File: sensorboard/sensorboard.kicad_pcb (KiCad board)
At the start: 4 copper layers, 100 x 50 mm, 244 parts, among them J1 Conn_01x03, J10 Conn_01x02_Male, J11 Conn_01x05_Male, J12 Conn_01x03, J13 Conn_01x03, J14 USB_C_Receptacle_USB2.0, J2 Conn_01x03, J3 Conn_01x03, J4 Conn_01x03, J5 Conn_01x03, J6 Conn_01x03, J7 Conn_01x03, J8 Conn_01x03, J9 Conn_01x02_Male, Q1 MMDT2222A, U1 ESP32-PICO-D4, U10 MAX31856, U11 MAX31856, U12 RT9025-25GSP, U13 ADS1219, U14 ADS1219, U15 ADS1219, U16 MAX31856, U17 MAX31856, U18 MAX31856, U19 LTC4411, U2 LTC4411, U20 SN65HVD230, U3 TPS61092RSAR, U4 MAX31856, U5 MAX31856, U6 MAX31856, U7 MAX31856, U8 CP2102-GMR-QFN28, U9 MAX31856

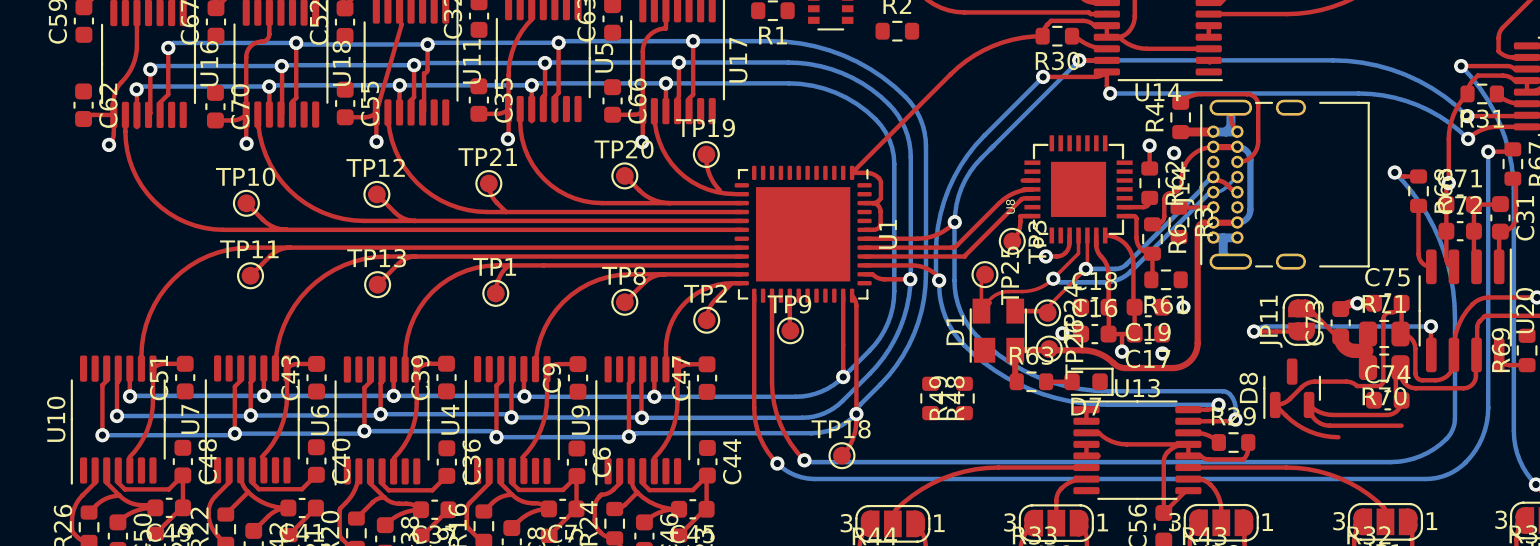
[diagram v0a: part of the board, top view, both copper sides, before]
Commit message: 3.3V connections and I2C capacitors
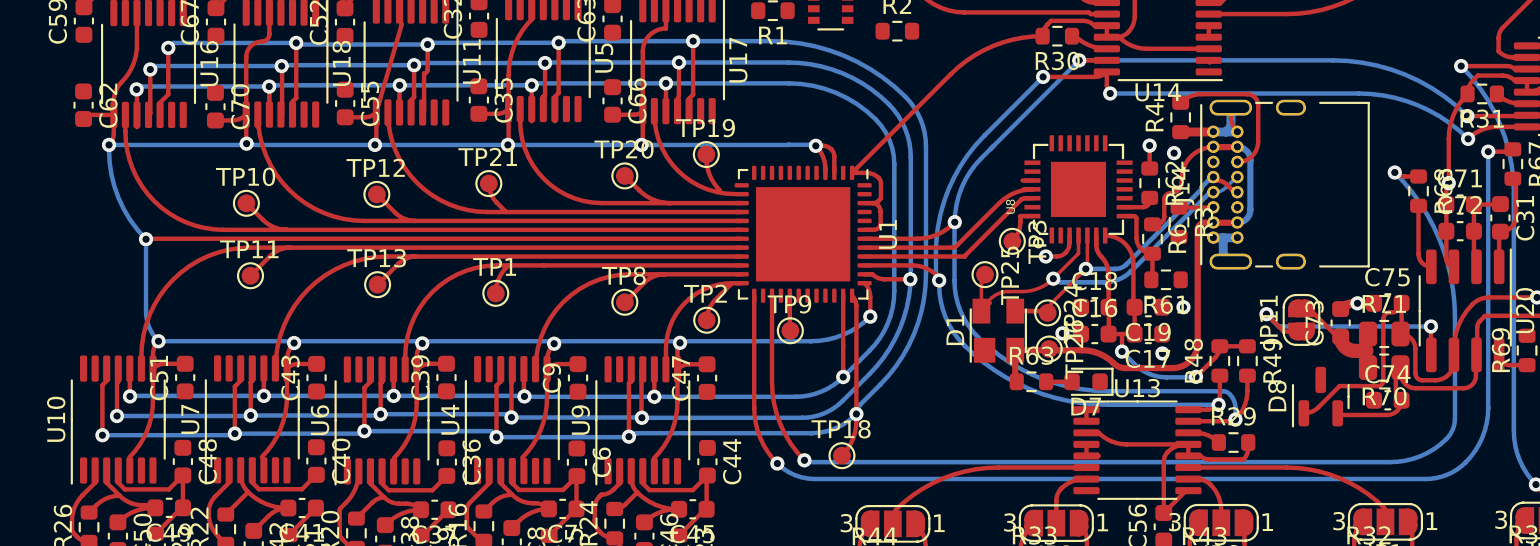
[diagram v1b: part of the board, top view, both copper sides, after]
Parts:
- moved R48 16.4 mm to (168.9, 61.7), turned to 90 degrees
- moved R49 16.0 mm to (170.5, 61.7), turned to -90 degrees
- moved D8 1.67 mm to (174.6, 63.7)
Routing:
- net +3V3: track 186.9 -> 334.9 mm, vias 8 -> 17
- net /CAN_HIGH: track 30.2 -> 22.7 mm
- net /CAN_LOW: track 36.2 -> 30.6 mm
- net /SDA: track 70.9 -> 73.5 mm
- net /SCL: track 68.2 -> 69.8 mm
- net /CAN/Vref: track 14.3 -> 13.5 mm

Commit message: update
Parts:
- moved R64 84.8 mm to (150.8, 85.9), turned to 180 degrees
- moved C24 83.5 mm to (167.3, 87.6), turned to 180 degrees
- moved U19 82.5 mm to (166.8, 90.2)
- moved U12 81.1 mm to (156.1, 88.2)
- moved C22 79.8 mm to (160.7, 88.5), turned to -90 degrees
- moved TP5 78.4 mm to (156.7, 48.7)
- moved C23 77.7 mm to (163.8, 88.4), turned to -90 degrees
- moved C20 77.4 mm to (150.7, 87.7)
- moved C21 76.7 mm to (150.7, 90.2)
- moved R66 74.1 mm to (162.9, 86.1)
- moved R65 67.4 mm to (162.3, 88.5), turned to 90 degrees
- moved C27 57.2 mm to (84.7, 61.8)
- moved C30 57.2 mm to (84.9, 63.7)
- moved C26 41.5 mm to (79.2, 62.3)
- moved C29 41.5 mm to (79.7, 64.5)
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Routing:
- net VBUS: track 34.2 -> 40.8 mm
- net Net-(C22-Pad2): track 0.00 -> 5.23 mm
- net Net-(C22-Pad1): track 0.00 -> 5.10 mm
- net Net-(R64-Pad1): track 0.00 -> 2.00 mm

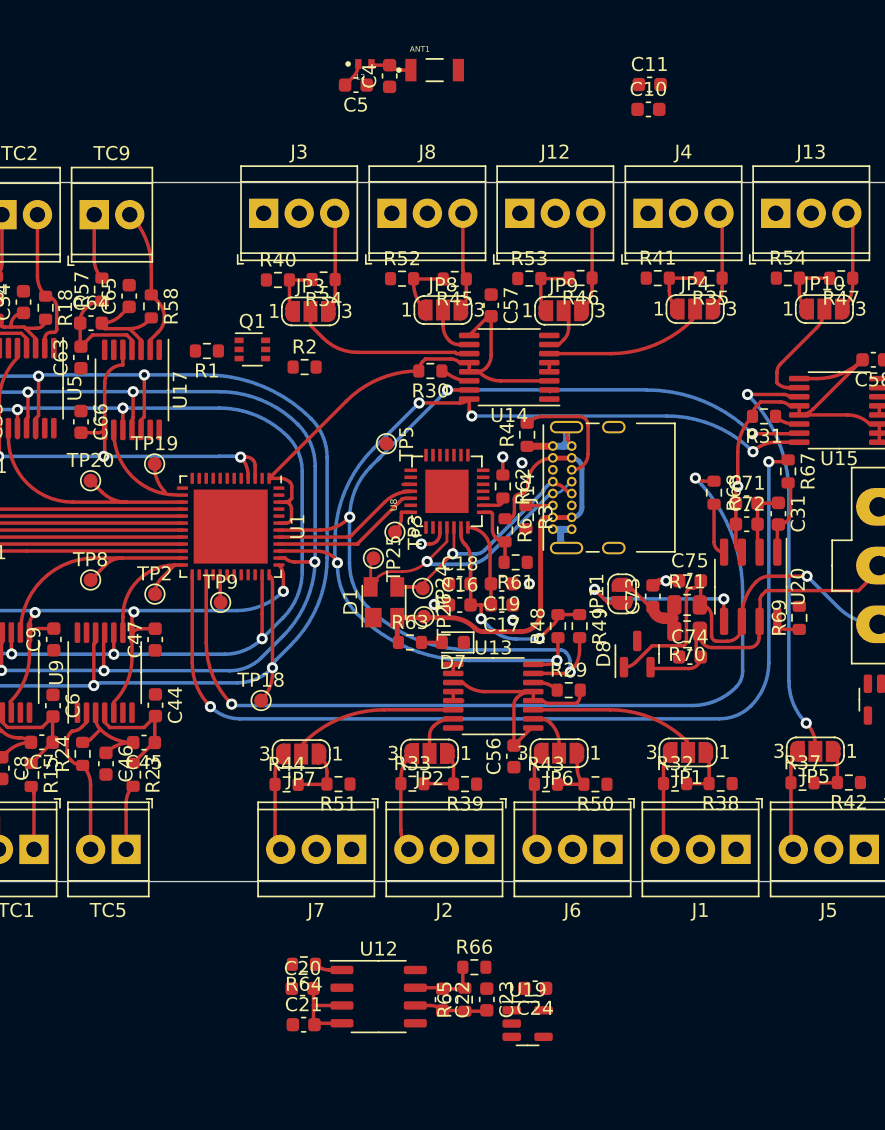
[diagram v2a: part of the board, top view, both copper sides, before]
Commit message: moved the U14 component and added component
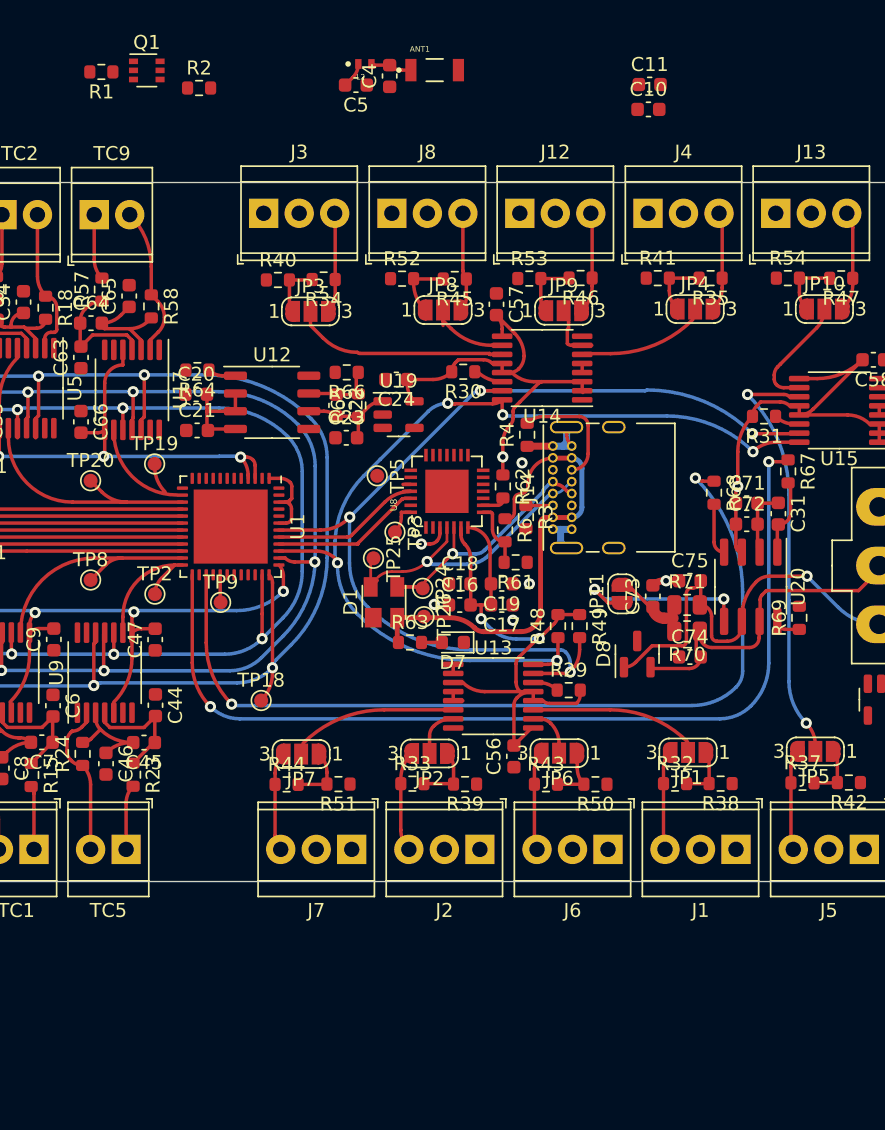
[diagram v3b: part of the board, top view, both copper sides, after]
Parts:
- moved C24 44.7 mm to (157.4, 44.1)
- moved U19 44.5 mm to (157.5, 46.6)
- moved R66 43.5 mm to (153.8, 43.6), turned to 180 degrees
- moved C22 43.2 mm to (153.1, 45.9)
- moved R64 43.2 mm to (143.1, 43.4)
- moved R65 43.2 mm to (154.7, 45.9)
- moved C20 43.2 mm to (143.1, 45.1)
- moved C21 43.2 mm to (143.1, 47.7)
- moved U12 43.2 mm to (148.5, 45.7)
- moved C23 41.4 mm to (153.8, 48.3), turned to 0 degrees
- moved R2 21.3 mm to (143.3, 23.2)
- moved Q1 21.3 mm to (139.5, 22.0)
- moved R1 21.3 mm to (136.3, 22.1)
- moved TP5 2.39 mm to (156.0, 51.0)
- moved U14 2.36 mm to (167.8, 43.3)
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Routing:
- net +3V3: track 334.9 -> 338.4 mm
- net /analogueI2C/AIN4: track 13.1 -> 15.6 mm
- net /analogueI2C/AIN6: track 10.9 -> 8.54 mm
- net /analogueI2C/AIN5: track 3.80 -> 5.87 mm
- net Net-(C22-Pad2): track 5.23 -> 7.29 mm
- net /SDA: track 73.5 -> 72.2 mm
- net VBUS: track 40.8 -> 42.1 mm
- net /analogueI2C/AIN7: track 3.43 -> 4.26 mm
- net /SCL: track 69.8 -> 69.3 mm

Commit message: transistor integration
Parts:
- moved TP6 142.5 mm to (156.5, 49.8)
- moved Q1 41.7 mm to (152.1, 61.8), turned to 90 degrees
- moved R1 41.6 mm to (149.8, 61.4), turned to 90 degrees
- moved R2 37.3 mm to (152.6, 59.3)
- moved L2 21.9 mm to (144.2, 40.4), turned to -90 degrees
- moved ANT1 20.6 mm to (144.6, 35.4), turned to 90 degrees
- moved C4 20.1 mm to (145.0, 38.6), turned to 180 degrees
- moved C5 20.1 mm to (145.7, 41.1), turned to -90 degrees
- moved TP9 10.7 mm to (153.9, 65.6)
- moved TP25 6.35 mm to (155.6, 63.2)
- moved TP18 5.22 mm to (144.5, 71.2)
- moved TP5 1.81 mm to (154.7, 52.2)
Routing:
- net VBUS: track 42.1 -> 72.1 mm, vias 0 -> 4
- net /EN: track 0.00 -> 27.6 mm, vias 0 -> 2
- net /BOOT: track 1.98 -> 20.4 mm
- net /RTS: track 0.55 -> 17.2 mm, vias 0 -> 2
- net /DTR: track 2.21 -> 15.7 mm
- net /LNA_IN: track 1.84 -> 11.2 mm
- net Net-(Q1-Pad2): track 0.00 -> 5.74 mm, vias 0 -> 2
- net /usb/Data+: track 21.5 -> 24.8 mm
- net /MOSI: track 153.7 -> 151.1 mm
- net /RXD: track 11.1 -> 13.1 mm
- net +3V3: track 338.4 -> 340.0 mm
- net Net-(Q1-Pad5): track 0.00 -> 1.57 mm

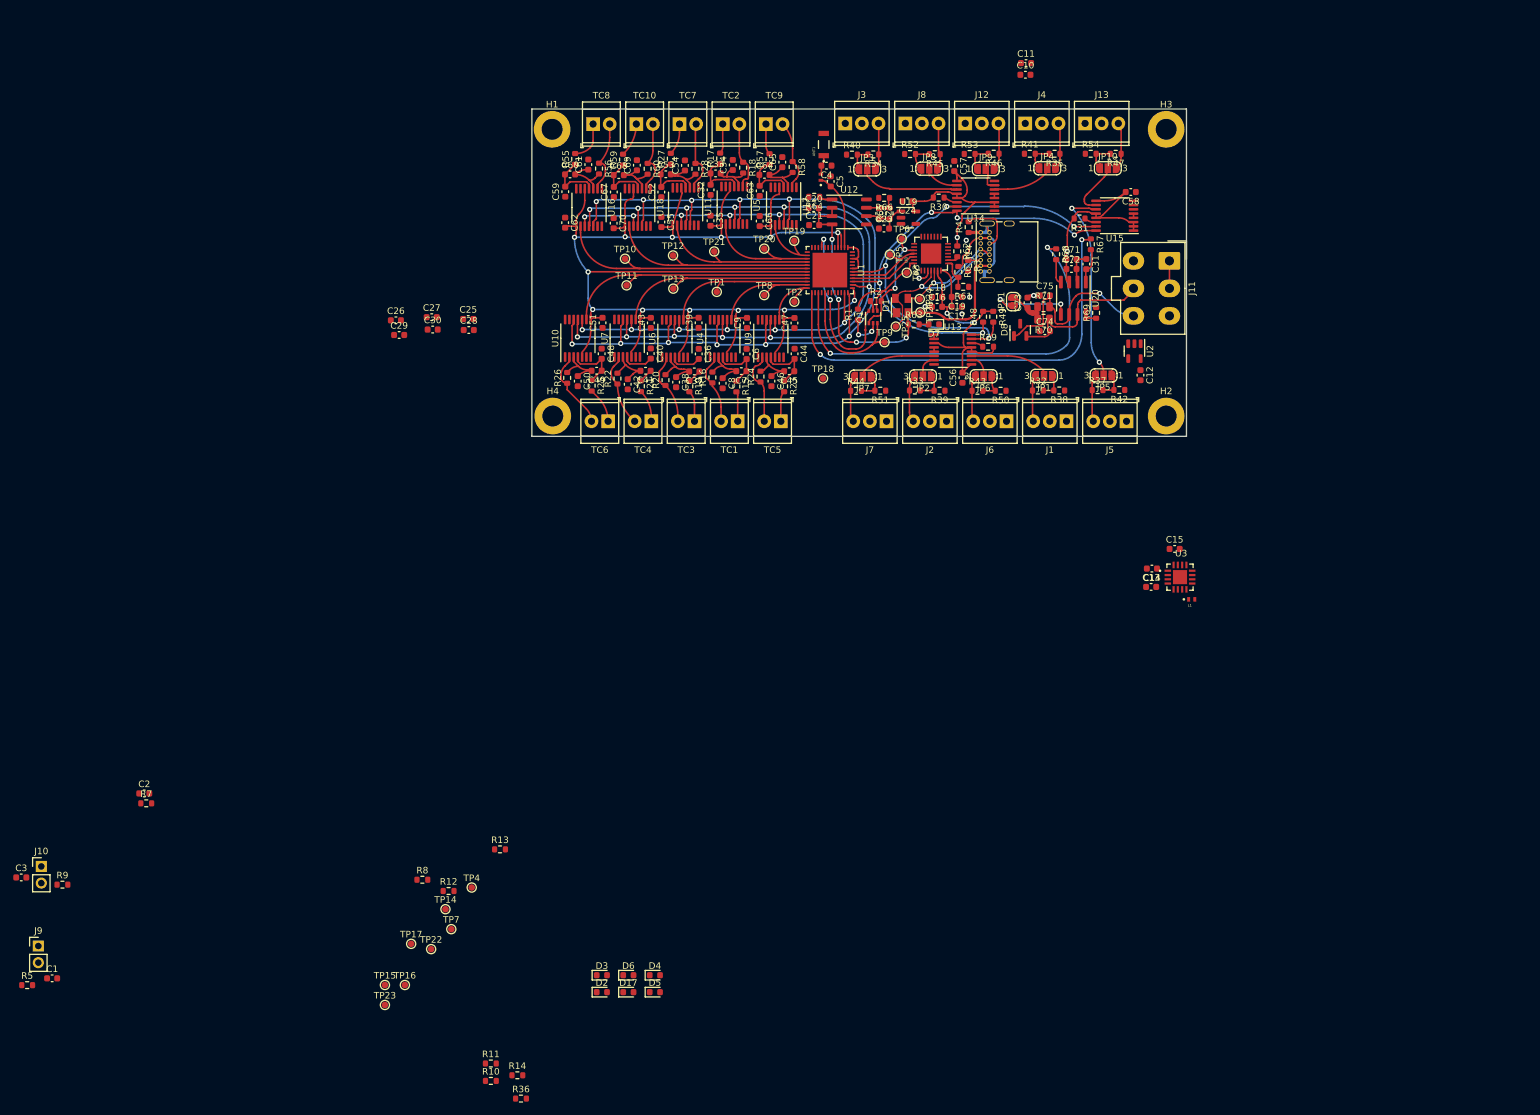
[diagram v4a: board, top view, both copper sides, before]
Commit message: connectors and changed capacitor values
capacitors for the connectors to 0.1uf
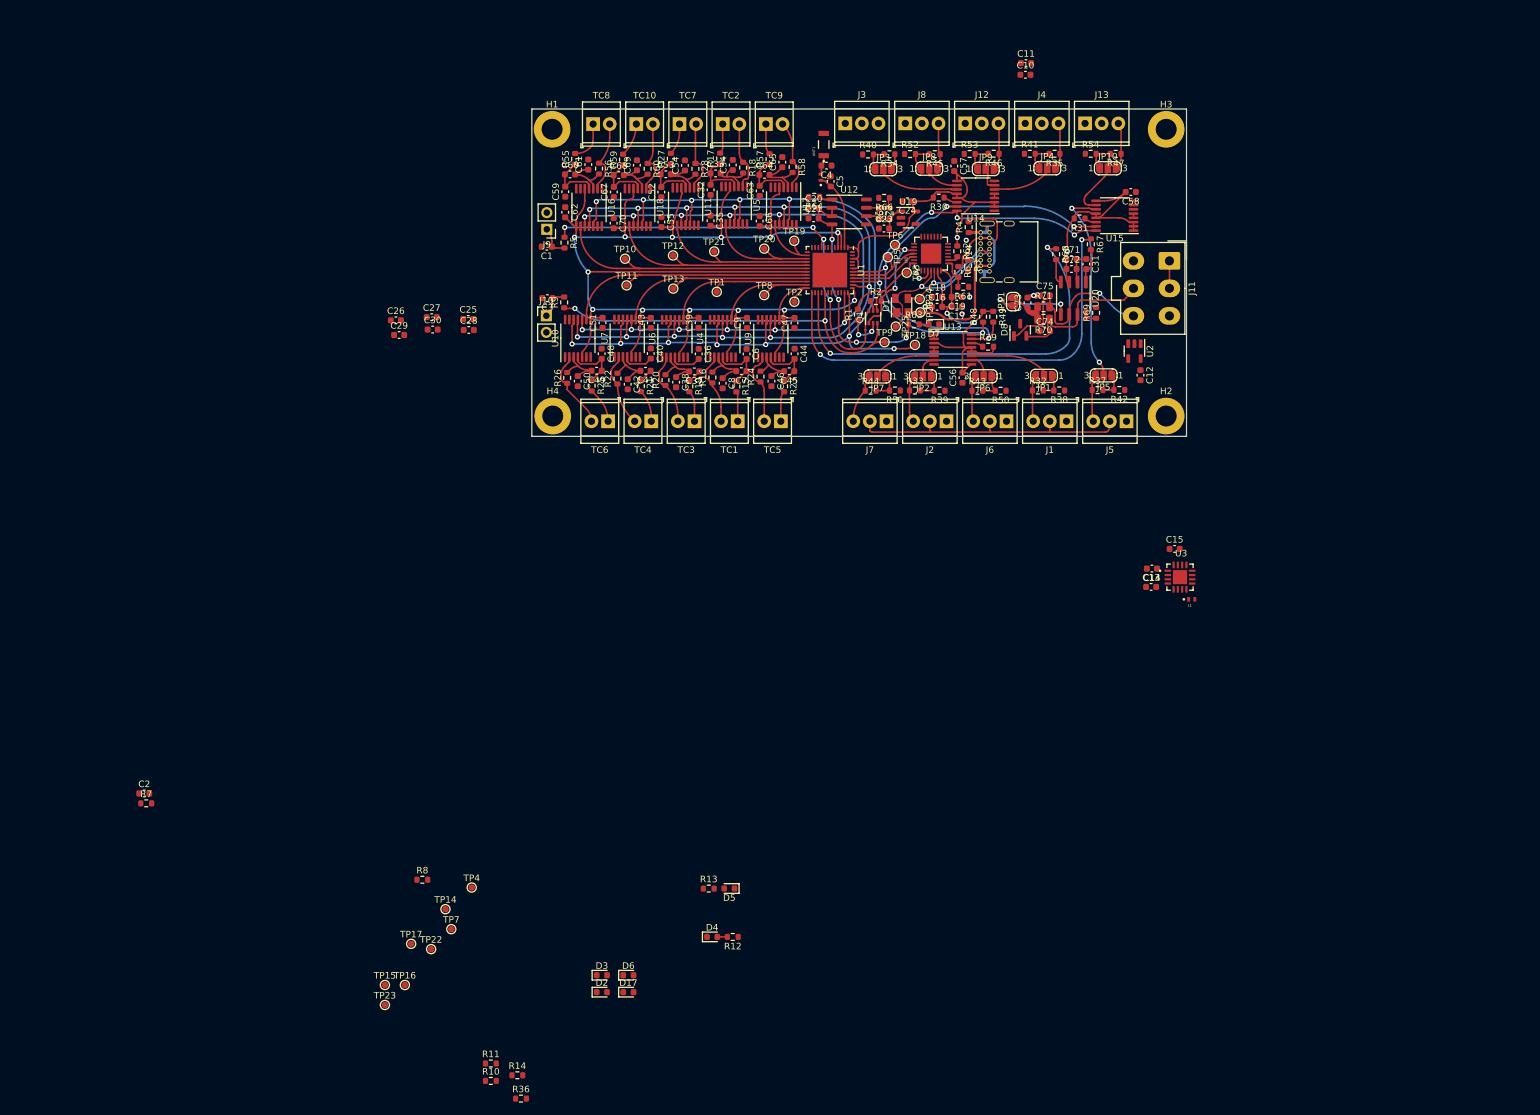
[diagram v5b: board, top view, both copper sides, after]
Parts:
- C1, C2, C3: value 1nF -> 0.1uF
- moved R5 140.0 mm to (105.0, 50.4), turned to -90 degrees
- moved C1 134.9 mm to (102.3, 51.0), turned to 180 degrees
- moved J9 134.2 mm to (102.3, 48.4), turned to 180 degrees
- moved C3 119.5 mm to (102.4, 58.9), turned to 180 degrees
- moved R9 117.4 mm to (104.9, 59.5), turned to 90 degrees
- moved J10 114.1 mm to (102.2, 61.6)
- moved R12 44.0 mm to (130.7, 156.5), turned to 180 degrees
- moved R13 32.4 mm to (127.0, 149.1)
- moved D5 19.5 mm to (130.2, 149.1), turned to 180 degrees
- moved TP18 14.9 mm to (158.5, 66.0)
- moved D4 10.5 mm to (127.5, 156.5)
- moved JP3 2.46 mm to (153.7, 39.2)
- moved R34 2.46 mm to (154.6, 36.9)
- moved R40 2.46 mm to (151.4, 36.9)
- moved R51 2.24 mm to (155.5, 73.0)
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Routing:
- net +5V: track 0.00 -> 44.5 mm
- net /EN: track 27.6 -> 69.5 mm, vias 2 -> 4
- net /BOOT: track 20.4 -> 60.8 mm, vias 0 -> 2
- net +3V3: track 340.0 -> 352.6 mm
- net /MOSI: track 151.1 -> 162.8 mm, vias 11 -> 12
- net Net-(C1-Pad1): track 0.00 -> 4.83 mm
- net Net-(C3-Pad1): track 0.00 -> 4.75 mm
- net Net-(J3-Pad3): track 7.15 -> 2.49 mm
- net /analogueI2C/AIN4: track 15.6 -> 12.7 mm
- net /analogueI2C/AIN3: track 11.3 -> 9.79 mm
- net Net-(D4-Pad2): track 0.00 -> 1.54 mm
